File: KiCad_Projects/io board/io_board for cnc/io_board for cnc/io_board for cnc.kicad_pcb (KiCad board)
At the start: 2 copper layers, 78.4 x 39.5 mm, 6 parts, among them J1 Conn_01x05_Female, J2 Conn_01x02_Female, SW1 SW_DIP_x01, SW2 SW_DIP_x01, SW3 SW_DIP_x01, SW4 SW_DIP_x01

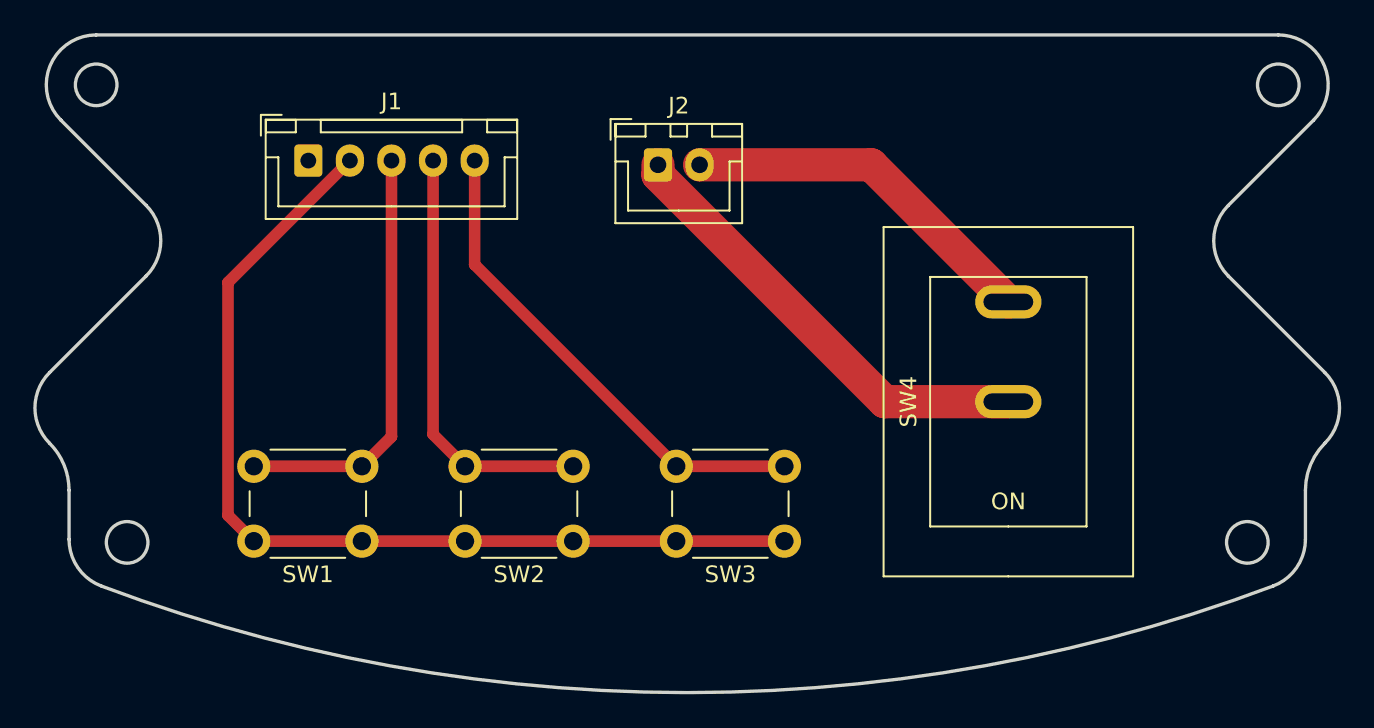
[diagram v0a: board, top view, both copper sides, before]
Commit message: 基板データの更新
IO基板
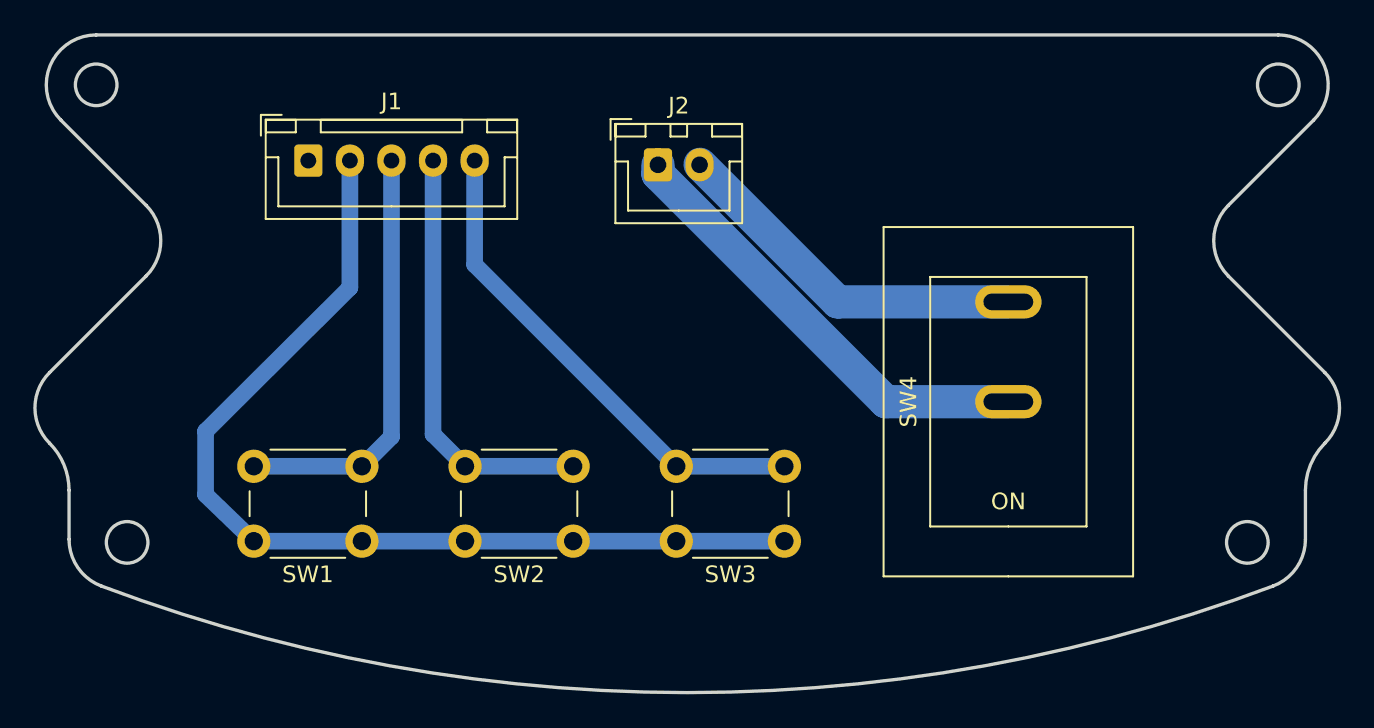
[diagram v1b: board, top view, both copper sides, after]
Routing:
- net +5V: track 58.5 -> 59.6 mm
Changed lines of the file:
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@@
   (gr_arc (start 111.845858 138.588448) (mid 110.435702 137.48804) (end 109.902462 135.780675) (layer "Edge.Cuts") (width 0.2))
   (gr_circle (center 182.598116 108.458859) (end 183.848116 108.458859) (layer "Edge.Cuts") (width 0.2) (fill none))
-  (segment (start 158.938409 127.508) (end 166.37 127.508) (width 2) (layer "F.Cu") (net 1))
-  (segment (start 145.308 113.877591) (end 158.938409 127.508) (width 2) (layer "F.Cu") (net 1))
-  (segment (start 145.308 113.267) (end 145.308 113.877591) (width 2) (layer "F.Cu") (net 1))
-  (segment (start 119.458489 120.340511) (end 119.458489 134.340489) (width 0.7) (layer "F.Cu") (net 2))
-  (segment (start 126.786 113.013) (end 119.458489 120.340511) (width 0.7) (layer "F.Cu") (net 2))
-  (segment (start 121.008 135.89) (end 152.908 135.89) (width 0.7) (layer "F.Cu") (net 2))
-  (segment (start 119.458489 134.340489) (end 121.008 135.89) (width 0.7) (layer "F.Cu") (net 2))
-  (segment (start 129.286 113.013) (end 129.286 129.612) (width 0.7) (layer "F.Cu") (net 3))
-  (segment (start 127.508 131.39) (end 121.008 131.39) (width 0.7) (layer "F.Cu") (net 3))
-  (segment (start 129.286 129.612) (end 127.508 131.39) (width 0.7) (layer "F.Cu") (net 3))
-  (segment (start 131.786 129.468) (end 133.708 131.39) (width 0.7) (layer "F.Cu") (net 4))
-  (segment (start 131.786 113.013) (end 131.786 129.468) (width 0.7) (layer "F.Cu") (net 4))
-  (segment (start 133.708 131.39) (end 140.208 131.39) (width 0.7) (layer "F.Cu") (net 4))
-  (segment (start 134.286 119.268) (end 146.408 131.39) (width 0.7) (layer "F.Cu") (net 5))
-  (segment (start 146.408 131.39) (end 152.908 131.39) (width 0.7) (layer "F.Cu") (net 5))
-  (segment (start 134.286 113.013) (end 134.286 119.268) (width 0.7) (layer "F.Cu") (net 5))
-  (segment (start 158.129 113.267) (end 166.37 121.508) (width 2) (layer "F.Cu") (net 6))
-  (segment (start 147.808 113.267) (end 158.129 113.267) (width 2) (layer "F.Cu") (net 6))
+  (segment (start 159.000542 127.508) (end 166.37 127.508) (width 2) (layer "B.Cu") (net 1))
+  (segment (start 145.308 113.267) (end 145.308 113.815458) (width 2) (layer "B.Cu") (net 1))
+  (segment (start 145.308 113.815458) (end 159.000542 127.508) (width 2) (layer "B.Cu") (net 1))
+  (segment (start 126.786 120.65) (end 118.11 129.286) (width 1) (layer "B.Cu") (net 2))
+  (segment (start 118.11 133.096) (end 121.008 135.89) (width 1) (layer "B.Cu") (net 2))
+  (segment (start 121.008 135.89) (end 152.908 135.89) (width 1) (layer "B.Cu") (net 2))
+  (segment (start 118.11 129.286) (end 118.11 133.096) (width 1) (layer "B.Cu") (net 2))
+  (segment (start 126.786 113.013) (end 126.786 120.65) (width 1) (layer "B.Cu") (net 2))
+  (segment (start 129.286 129.612) (end 127.508 131.39) (width 1) (layer "B.Cu") (net 3))
+  (segment (start 129.286 113.013) (end 129.286 129.612) (width 1) (layer "B.Cu") (net 3))
+  (segment (start 127.508 131.39) (end 121.008 131.39) (width 1) (layer "B.Cu") (net 3))
+  (segment (start 131.786 129.468) (end 133.708 131.39) (width 1) (layer "B.Cu") (net 4))
+  (segment (start 131.786 113.013) (end 131.786 129.468) (width 1) (layer "B.Cu") (net 4))
+  (segment (start 140.208 131.39) (end 133.708 131.39) (width 1) (layer "B.Cu") (net 4))
+  (segment (start 134.286 119.268) (end 146.408 131.39) (width 1) (layer "B.Cu") (net 5))
+  (segment (start 134.286 113.013) (end 134.286 119.268) (width 1) (layer "B.Cu") (net 5))
+  (segment (start 146.408 131.39) (end 152.908 131.39) (width 1) (layer "B.Cu") (net 5))
+  (segment (start 166.37 121.508) (end 156.111134 121.508) (width 2) (layer "B.Cu") (net 6))
+  (segment (start 156.111134 121.508) (end 147.839067 113.235933) (width 2) (layer "B.Cu") (net 6))
   (group "" (id fe2e0ca8-c07a-43f5-8244-13ab30d5fbde)
     (members

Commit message: 部内大会用プログラムの作成
部内大会というか、北九州オープンくらいまでのプログラムが入ってます。
カメラ・IR_ring・Line_ringの制御。
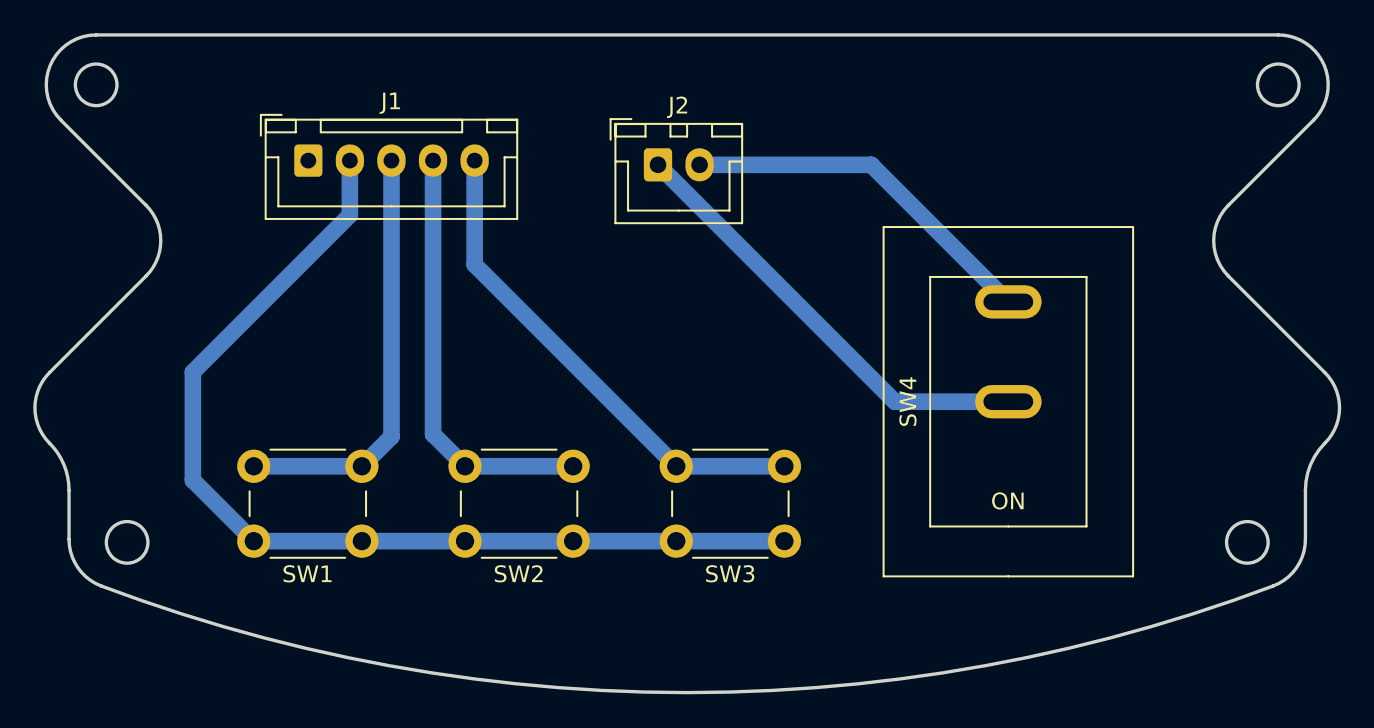
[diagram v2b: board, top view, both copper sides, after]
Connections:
- J1 pad 1: GND -> GND1
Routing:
- net +5V: track 59.6 -> 60.2 mm
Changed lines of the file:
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@@
     (pad_to_mask_clearance 0)
     (pcbplotparams
-      (layerselection 0x00010fc_ffffffff)
+      (layerselection 0x0001000_ffffffff)
       (disableapertmacros false)
       (usegerberextensions false)
-      (usegerberattributes true)
-      (usegerberadvancedattributes true)
-      (creategerberjobfile true)
+      (usegerberattributes false)
+      (usegerberadvancedattributes false)
+      (creategerberjobfile false)
       (svguseinch false)
       (svgprecision 6)
@@
       (outputformat 1)
       (mirror false)
-      (drillshape 1)
+      (drillshape 0)
       (scaleselection 1)
-      (outputdirectory "")
+      (outputdirectory "GBR_FILE/")
     )
   )
@@
   (net 5 "SW3")
   (net 6 "+7.5V")
+  (net 7 "GND1")
   (footprint "Button_Switch_THT:SW_PUSH_6mm_H5mm" (layer "F.Cu")
     (at 127.508 135.89 180)
@@
     (fp_line (start 0 -1.35) (end 0.625 -2.35) (layer "F.Fab") (width 0.1))
     (fp_line (start 4.95 3.4) (end 4.95 -2.35) (layer "F.Fab") (width 0.1))
-    (pad "1" thru_hole roundrect (at 0 0) (size 1.7 2) (drill 1) (layers *.Cu *.Mask) (roundrect_rratio 0.147059)
+    (pad "1" thru_hole roundrect (at 0 0) (size 1.7 2) (drill 1) (layers *.Cu *.Mask) (roundrect_rratio 0.1470588235)
       (net 1 "GND") (pinfunction "Pin_1") (pintype "passive"))
     (pad "2" thru_hole oval (at 2.5 0) (size 1.7 2) (drill 1) (layers *.Cu *.Mask)
@@
     (fp_line (start -2.45 3.4) (end 12.45 3.4) (layer "F.Fab") (width 0.1))
     (fp_line (start -2.45 -2.35) (end -2.45 3.4) (layer "F.Fab") (width 0.1))
-    (pad "1" thru_hole roundrect (at 0 0) (size 1.7 1.95) (drill 0.95) (layers *.Cu *.Mask) (roundrect_rratio 0.147059)
-      (net 1 "GND") (pinfunction "Pin_1") (pintype "passive"))
+    (pad "1" thru_hole roundrect (at 0 0) (size 1.7 1.95) (drill 0.95) (layers *.Cu *.Mask) (roundrect_rratio 0.1470588235)
+      (net 7 "GND1") (pinfunction "Pin_1") (pintype "passive"))
     (pad "2" thru_hole oval (at 2.5 0) (size 1.7 1.95) (drill 0.95) (layers *.Cu *.Mask)
       (net 2 "+5V") (pinfunction "Pin_2") (pintype "passive"))
@@
   (gr_arc (start 111.845858 138.588448) (mid 110.435702 137.48804) (end 109.902462 135.780675) (layer "Edge.Cuts") (width 0.2))
   (gr_circle (center 182.598116 108.458859) (end 183.848116 108.458859) (layer "Edge.Cuts") (width 0.2) (fill none))
-  (segment (start 159.000542 127.508) (end 166.37 127.508) (width 2) (layer "B.Cu") (net 1))
-  (segment (start 145.308 113.267) (end 145.308 113.815458) (width 2) (layer "B.Cu") (net 1))
-  (segment (start 145.308 113.815458) (end 159.000542 127.508) (width 2) (layer "B.Cu") (net 1))
-  (segment (start 126.786 120.65) (end 118.11 129.286) (width 1) (layer "B.Cu") (net 2))
-  (segment (start 118.11 133.096) (end 121.008 135.89) (width 1) (layer "B.Cu") (net 2))
-  (segment (start 121.008 135.89) (end 152.908 135.89) (width 1) (layer "B.Cu") (net 2))
-  (segment (start 118.11 129.286) (end 118.11 133.096) (width 1) (layer "B.Cu") (net 2))
-  (segment (start 126.786 113.013) (end 126.786 120.65) (width 1) (layer "B.Cu") (net 2))
-  (segment (start 129.286 129.612) (end 127.508 131.39) (width 1) (layer "B.Cu") (net 3))
-  (segment (start 129.286 113.013) (end 129.286 129.612) (width 1) (layer "B.Cu") (net 3))
+  (segment (start 159.549 127.508) (end 166.37 127.508) (width 1) (layer "B.Cu") (net 1))
+  (segment (start 145.308 113.267) (end 159.549 127.508) (width 1) (layer "B.Cu") (net 1))
+  (segment (start 121.008 135.89) (end 127.508 135.89) (width 1) (layer "B.Cu") (net 2))
+  (segment (start 117.348 125.73) (end 117.348 132.23) (width 1) (layer "B.Cu") (net 2))
+  (segment (start 140.208 135.89) (end 146.408 135.89) (width 1) (layer "B.Cu") (net 2))
+  (segment (start 146.408 135.89) (end 152.908 135.89) (width 1) (layer "B.Cu") (net 2))
+  (segment (start 117.348 132.23) (end 121.008 135.89) (width 1) (layer "B.Cu") (net 2))
+  (segment (start 127.508 135.89) (end 133.708 135.89) (width 1) (layer "B.Cu") (net 2))
+  (segment (start 126.786 113.013) (end 126.786 116.292) (width 1) (layer "B.Cu") (net 2))
+  (segment (start 126.786 116.292) (end 117.348 125.73) (width 1) (layer "B.Cu") (net 2))
+  (segment (start 133.708 135.89) (end 140.208 135.89) (width 1) (layer "B.Cu") (net 2))
   (segment (start 127.508 131.39) (end 121.008 131.39) (width 1) (layer "B.Cu") (net 3))
-  (segment (start 131.786 129.468) (end 133.708 131.39) (width 1) (layer "B.Cu") (net 4))
-  (segment (start 131.786 113.013) (end 131.786 129.468) (width 1) (layer "B.Cu") (net 4))
+  (segment (start 129.286 129.612) (end 129.286 113.013) (width 1) (layer "B.Cu") (net 3))
+  (segment (start 127.508 131.39) (end 129.286 129.612) (width 1) (layer "B.Cu") (net 3))
   (segment (start 140.208 131.39) (end 133.708 131.39) (width 1) (layer "B.Cu") (net 4))
-  (segment (start 134.286 119.268) (end 146.408 131.39) (width 1) (layer "B.Cu") (net 5))
-  (segment (start 134.286 113.013) (end 134.286 119.268) (width 1) (layer "B.Cu") (net 5))
-  (segment (start 146.408 131.39) (end 152.908 131.39) (width 1) (layer "B.Cu") (net 5))
-  (segment (start 166.37 121.508) (end 156.111134 121.508) (width 2) (layer "B.Cu") (net 6))
-  (segment (start 156.111134 121.508) (end 147.839067 113.235933) (width 2) (layer "B.Cu") (net 6))
+  (segment (start 131.786 129.468) (end 131.786 113.013) (width 1) (layer "B.Cu") (net 4))
+  (segment (start 133.708 131.39) (end 131.786 129.468) (width 1) (layer "B.Cu") (net 4))
+  (segment (start 152.908 131.39) (end 146.408 131.39) (width 1) (layer "B.Cu") (net 5))
+  (segment (start 134.286 119.268) (end 134.286 113.013) (width 1) (layer "B.Cu") (net 5))
+  (segment (start 146.408 131.39) (end 134.286 119.268) (width 1) (layer "B.Cu") (net 5))
+  (segment (start 158.129 113.267) (end 166.37 121.508) (width 1) (layer "B.Cu") (net 6))
+  (segment (start 147.808 113.267) (end 158.129 113.267) (width 1) (layer "B.Cu") (net 6))
   (group "" (id fe2e0ca8-c07a-43f5-8244-13ab30d5fbde)
     (members
